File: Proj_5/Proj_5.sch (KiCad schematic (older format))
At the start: 1 part

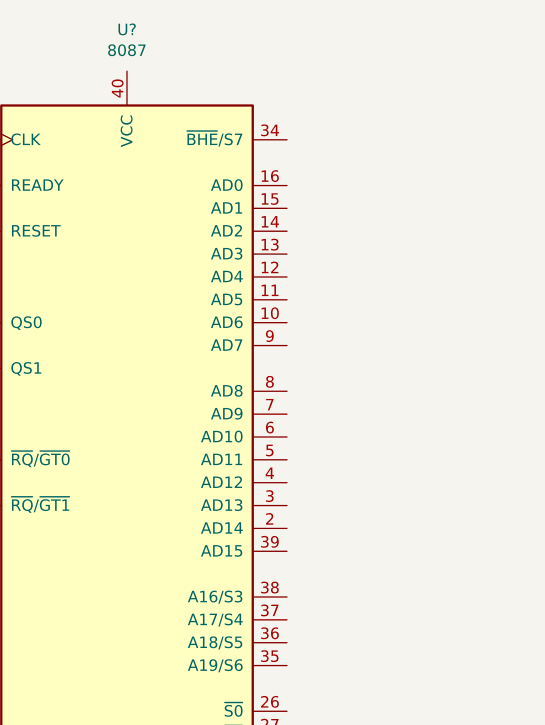
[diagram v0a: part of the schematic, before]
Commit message: Added Address Bus
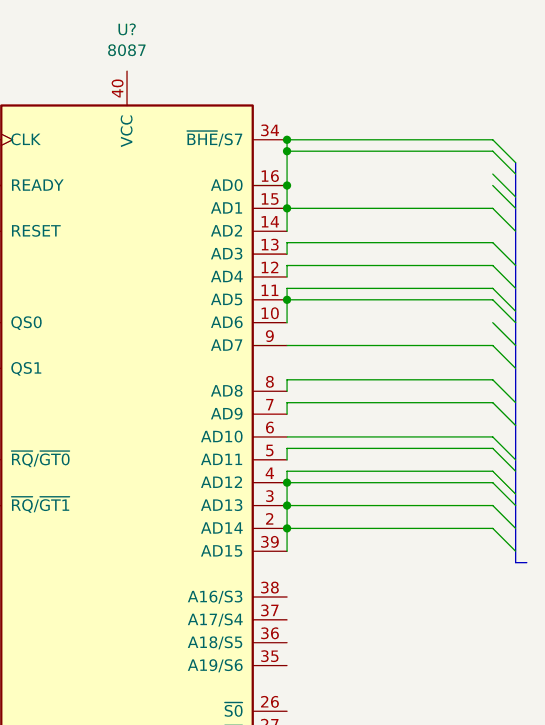
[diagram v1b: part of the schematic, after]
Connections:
- net at U?.10 (AD6): now also U?.11 (AD5)
- net at U?.14 (AD2): now also U?.15 (AD1), U?.16 (AD0), U?.34 (~BHE~/S7)
- net at U?.2 (AD14): now also U?.3 (AD13), U?.39 (AD15), U?.4 (AD12)
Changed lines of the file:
@@
 	1    0    0    -1
 $EndComp
+Wire Bus Line
+	3500 3250 3550 3250
+Entry Wire Line
+	3400 2300 3500 2400
+Entry Wire Line
+	3400 2450 3500 2550
+Entry Wire Line
+	3400 2550 3500 2650
+Entry Wire Line
+	3400 2700 3500 2800
+Entry Wire Line
+	3400 2750 3500 2850
+Entry Wire Line
+	3400 2850 3500 2950
+Entry Wire Line
+	3400 2900 3500 3000
+Entry Wire Line
+	3400 3000 3500 3100
+Entry Wire Line
+	3400 3100 3500 3200
+Entry Wire Line
+	3400 2200 3500 2300
+Entry Wire Line
+	3400 2100 3500 2200
+Entry Wire Line
+	3400 2050 3500 2150
+Entry Wire Line
+	3400 1950 3500 2050
+Entry Wire Line
+	3400 1850 3500 1950
+Entry Wire Line
+	3400 1700 3500 1800
+Entry Wire Line
+	3400 1600 3500 1700
+Entry Wire Line
+	3400 1450 3500 1550
+Entry Wire Line
+	3400 1400 3500 1500
+Entry Wire Line
+	3400 1550 3500 1650
+Wire Wire Line
+	3400 1400 2500 1400
+Connection ~ 2500 1400
+Wire Wire Line
+	3400 1450 2500 1450
+Wire Wire Line
+	2500 1400 2500 1450
+Connection ~ 2500 1450
+Wire Wire Line
+	2500 1450 2500 1600
+Connection ~ 2500 1600
+Wire Wire Line
+	2500 1600 2500 1700
+Wire Wire Line
+	3400 1850 2500 1850
+Wire Wire Line
+	2500 1850 2500 1900
+Wire Wire Line
+	3400 1700 2500 1700
+Wire Wire Line
+	2500 1700 2500 1800
+Connection ~ 2500 1700
+Wire Wire Line
+	3400 1950 2500 1950
+Wire Wire Line
+	2500 1950 2500 2000
+Wire Wire Line
+	3400 2050 2500 2050
+Wire Wire Line
+	2500 2050 2500 2100
+Wire Wire Line
+	3400 2100 2500 2100
+Wire Wire Line
+	2500 2100 2500 2200
+Connection ~ 2500 2100
+Wire Wire Line
+	3400 2300 2500 2300
+Wire Wire Line
+	3400 2450 2500 2450
+Wire Wire Line
+	2500 2450 2500 2500
+Wire Wire Line
+	3400 2550 2500 2550
+Wire Wire Line
+	2500 2550 2500 2600
+Wire Wire Line
+	3400 2700 2500 2700
+Wire Wire Line
+	3400 2750 2500 2750
+Wire Wire Line
+	2500 2750 2500 2800
+Wire Wire Line
+	3400 2850 2500 2850
+Wire Wire Line
+	2500 2850 2500 2900
+Wire Wire Line
+	3400 2900 2500 2900
+Wire Wire Line
+	2500 2900 2500 3000
+Connection ~ 2500 2900
+Wire Wire Line
+	3400 3000 2500 3000
+Wire Wire Line
+	2500 3000 2500 3100
+Connection ~ 2500 3000
+Wire Wire Line
+	3400 3100 2500 3100
+Wire Wire Line
+	2500 3100 2500 3200
+Wire Bus Line
+	3500 1500 3500 3250
+Connection ~ 2500 3100
 $EndSCHEMATC

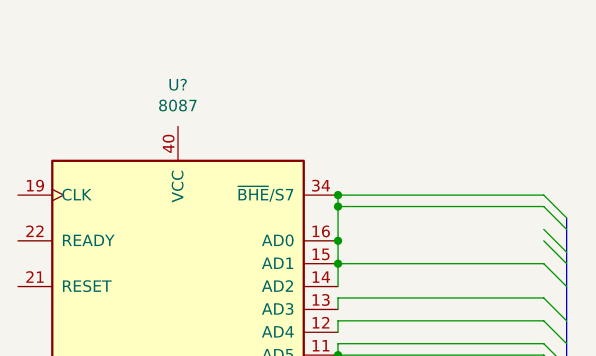
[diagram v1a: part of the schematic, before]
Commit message: Added Power to 8087
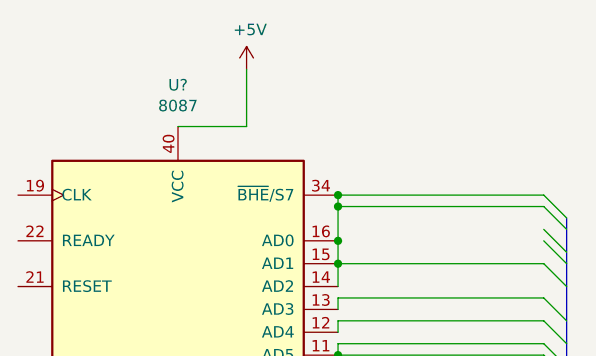
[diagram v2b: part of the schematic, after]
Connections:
- net +5V: now reaches U?.40 (VCC)
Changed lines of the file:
@@
 Wire Wire Line
 	2500 3100 2500 3200
+Connection ~ 2500 3100
+$Comp
+L power:+5V #PWR?
+U 1 1 5E90A12F
+P 2100 850
+F 0 "#PWR?" H 2100 700 50  0001 C CNN
+F 1 "+5V" H 2115 1023 50  0000 C CNN
+F 2 "" H 2100 850 50  0001 C CNN
+F 3 "" H 2100 850 50  0001 C CNN
+	1    2100 850
+	1    0    0    -1
+$EndComp
+Wire Wire Line
+	1800 1100 2100 1100
+Wire Wire Line
+	2100 1100 2100 850
 Wire Bus Line
 	3500 1500 3500 3250
-Connection ~ 2500 3100
 $EndSCHEMATC

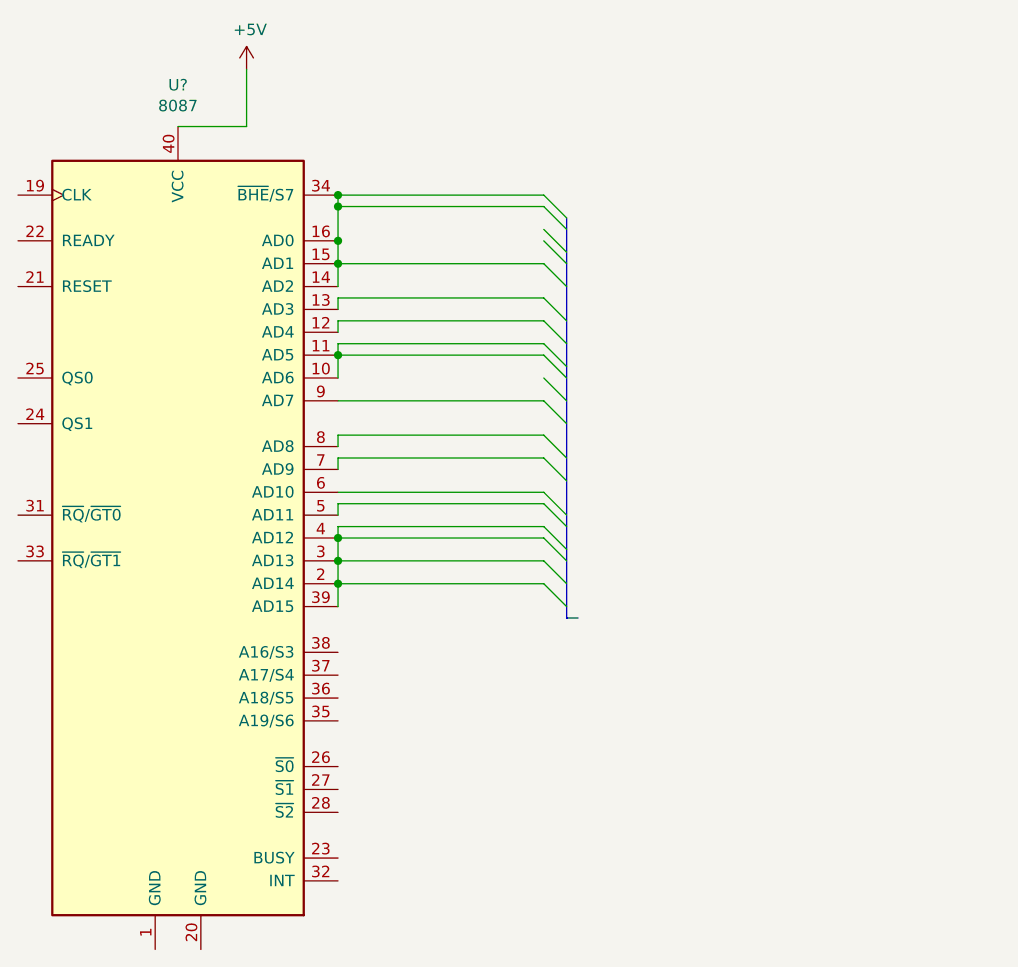
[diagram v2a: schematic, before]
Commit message: Added a clock circuit
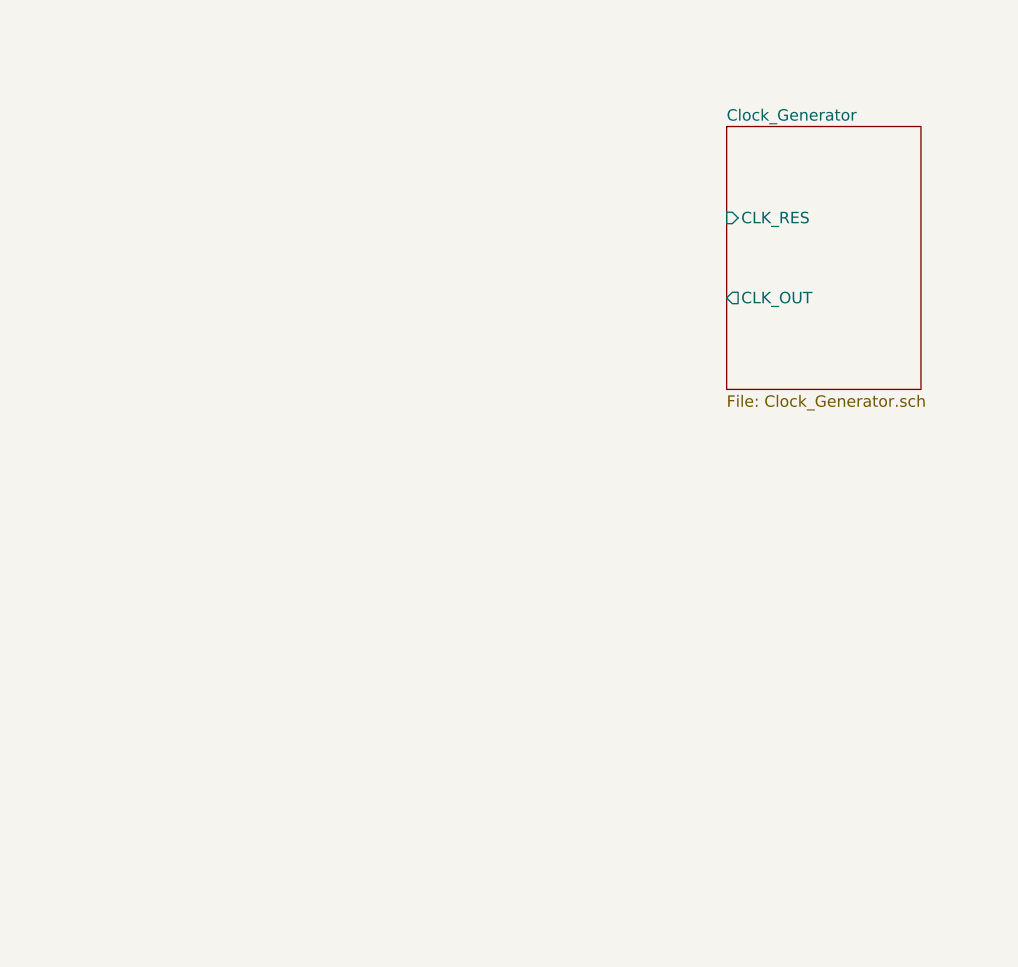
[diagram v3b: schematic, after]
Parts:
- removed U?: 8087, Package_DIP:DIP-40_W15.24mm, symbol MCU_Intel:8087
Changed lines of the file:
@@
 EELAYER 30 0
 EELAYER END
-$Descr A4 11693 8268
+$Descr User 19685 19685
 encoding utf-8
-Sheet 1 1
+Sheet 1 2
 Title ""
 Date ""
@@
 Comment4 ""
 $EndDescr
-$Comp
-L MCU_Intel:8087 U?
-U 1 1 5E90928D
-P 1800 2900
-F 0 "U?" H 1800 4881 50  0000 C CNN
-F 1 "8087" H 1800 4790 50  0000 C CNN
-F 2 "Package_DIP:DIP-40_W15.24mm" H 1850 3000 50  0001 C CIN
-F 3 "http://datasheets.chipdb.org/Intel/x86/808x/datashts/8087/205835-007.pdf" H 1800 2950 50  0001 C CNN
-	1    1800 2900
-	1    0    0    -1
-$EndComp
-Wire Bus Line
-	3500 3250 3550 3250
-Entry Wire Line
-	3400 2300 3500 2400
-Entry Wire Line
-	3400 2450 3500 2550
-Entry Wire Line
-	3400 2550 3500 2650
-Entry Wire Line
-	3400 2700 3500 2800
-Entry Wire Line
-	3400 2750 3500 2850
-Entry Wire Line
-	3400 2850 3500 2950
-Entry Wire Line
-	3400 2900 3500 3000
-Entry Wire Line
-	3400 3000 3500 3100
-Entry Wire Line
-	3400 3100 3500 3200
-Entry Wire Line
-	3400 2200 3500 2300
-Entry Wire Line
-	3400 2100 3500 2200
-Entry Wire Line
-	3400 2050 3500 2150
-Entry Wire Line
-	3400 1950 3500 2050
-Entry Wire Line
-	3400 1850 3500 1950
-Entry Wire Line
-	3400 1700 3500 1800
-Entry Wire Line
-	3400 1600 3500 1700
-Entry Wire Line
-	3400 1450 3500 1550
-Entry Wire Line
-	3400 1400 3500 1500
-Entry Wire Line
-	3400 1550 3500 1650
-Wire Wire Line
-	3400 1400 2500 1400
-Connection ~ 2500 1400
-Wire Wire Line
-	3400 1450 2500 1450
-Wire Wire Line
-	2500 1400 2500 1450
-Connection ~ 2500 1450
-Wire Wire Line
-	2500 1450 2500 1600
-Connection ~ 2500 1600
-Wire Wire Line
-	2500 1600 2500 1700
-Wire Wire Line
-	3400 1850 2500 1850
-Wire Wire Line
-	2500 1850 2500 1900
-Wire Wire Line
-	3400 1700 2500 1700
-Wire Wire Line
-	2500 1700 2500 1800
-Connection ~ 2500 1700
-Wire Wire Line
-	3400 1950 2500 1950
-Wire Wire Line
-	2500 1950 2500 2000
-Wire Wire Line
-	3400 2050 2500 2050
-Wire Wire Line
-	2500 2050 2500 2100
-Wire Wire Line
-	3400 2100 2500 2100
-Wire Wire Line
-	2500 2100 2500 2200
-Connection ~ 2500 2100
-Wire Wire Line
-	3400 2300 2500 2300
-Wire Wire Line
-	3400 2450 2500 2450
-Wire Wire Line
-	2500 2450 2500 2500
-Wire Wire Line
-	3400 2550 2500 2550
-Wire Wire Line
-	2500 2550 2500 2600
-Wire Wire Line
-	3400 2700 2500 2700
-Wire Wire Line
-	3400 2750 2500 2750
-Wire Wire Line
-	2500 2750 2500 2800
-Wire Wire Line
-	3400 2850 2500 2850
-Wire Wire Line
-	2500 2850 2500 2900
-Wire Wire Line
-	3400 2900 2500 2900
-Wire Wire Line
-	2500 2900 2500 3000
-Connection ~ 2500 2900
-Wire Wire Line
-	3400 3000 2500 3000
-Wire Wire Line
-	2500 3000 2500 3100
-Connection ~ 2500 3000
-Wire Wire Line
-	3400 3100 2500 3100
-Wire Wire Line
-	2500 3100 2500 3200
-Connection ~ 2500 3100
-$Comp
-L power:+5V #PWR?
-U 1 1 5E90A12F
-P 2100 850
-F 0 "#PWR?" H 2100 700 50  0001 C CNN
-F 1 "+5V" H 2115 1023 50  0000 C CNN
-F 2 "" H 2100 850 50  0001 C CNN
-F 3 "" H 2100 850 50  0001 C CNN
-	1    2100 850
-	1    0    0    -1
-$EndComp
-Wire Wire Line
-	1800 1100 2100 1100
-Wire Wire Line
-	2100 1100 2100 850
-Wire Bus Line
-	3500 1500 3500 3250
+$Sheet
+S 4200 1100 850  1150
+U 5E9E2E0E
+F0 "Clock_Generator" 50
+F1 "Clock_Generator.sch" 50
+F2 "CLK_RES" I L 4200 1500 50
+F3 "CLK_OUT" O L 4200 1850 50
+$EndSheet
 $EndSCHEMATC

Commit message: Added Schematics, finish SRAM and 8279
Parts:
- added U?: 8086_Min_Mode, Package_DIP:DIP-40_W15.24mm, symbol MCU_Intel:8086_Min_Mode
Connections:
- net Clock_Generator/CLK_OUT: now also U?.19 (CLK)
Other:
- note added: "Ryan Bugianesi and Collin Mood\n"
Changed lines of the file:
@@
 $Descr User 19685 19685
 encoding utf-8
-Sheet 1 2
+Sheet 1 9
 Title ""
 Date ""
@@
 $EndDescr
 $Sheet
-S 4200 1100 850  1150
+S 1150 800  850  1150
 U 5E9E2E0E
 F0 "Clock_Generator" 50
 F1 "Clock_Generator.sch" 50
-F2 "CLK_RES" I L 4200 1500 50
-F3 "CLK_OUT" O L 4200 1850 50
+F2 "CLK_RES" I L 1150 1200 50
+F3 "CLK_OUT" O L 1150 1550 50
 $EndSheet
+$Comp
+L MCU_Intel:8086_Min_Mode U?
+U 1 1 5E99BD91
+P 3200 4050
+F 0 "U?" H 3200 6031 50  0000 C CNN
+F 1 "8086_Min_Mode" H 3200 5940 50  0000 C CNN
+F 2 "Package_DIP:DIP-40_W15.24mm" H 3250 4150 50  0001 C CIN
+F 3 "http://datasheets.chipdb.org/Intel/x86/808x/datashts/8086/231455-006.pdf" H 3200 4100 50  0001 C CNN
+	1    3200 4050
+	1    0    0    -1
+$EndComp
+Wire Wire Line
+	1150 1550 750  1550
+Wire Wire Line
+	750  1550 750  2550
+Wire Wire Line
+	750  2550 2500 2550
+$Sheet
+S 13550 4000 2500 1950
+U 5EA0416B
+F0 "8255s" 157
+F1 "8255s.sch" 157
+$EndSheet
+$Sheet
+S 13500 1000 2500 2250
+U 5EA045EA
+F0 "CMOS Flash" 157
+F1 "CMOS-28F010s.sch" 157
+$EndSheet
+$Sheet
+S 13550 6850 2600 2600
+U 5EA98353
+F0 "SRAM Memory" 256
+F1 "CY7C199.sch" 256
+$EndSheet
+$Sheet
+S 13750 11050 2450 2500
+U 5EA98A67
+F0 "16550 UART" 256
+F1 "16550UART.sch" 256
+$EndSheet
+$Sheet
+S 8200 14600 3250 2700
+U 5EA99014
+F0 "8259" 256
+F1 "8259.sch" 256
+$EndSheet
+$Sheet
+S 13850 14800 3400 2350
+U 5EA99146
+F0 "8254" 256
+F1 "8254.sch" 256
+$EndSheet
+$Sheet
+S 3900 14900 3050 2250
+U 5EA993EC
+F0 "8279" 256
+F1 "8279.sch" 256
+$EndSheet
+Text Notes 14950 18250 0    169  ~ 0
+Ryan Bugianesi and Collin Mood\n
 $EndSCHEMATC

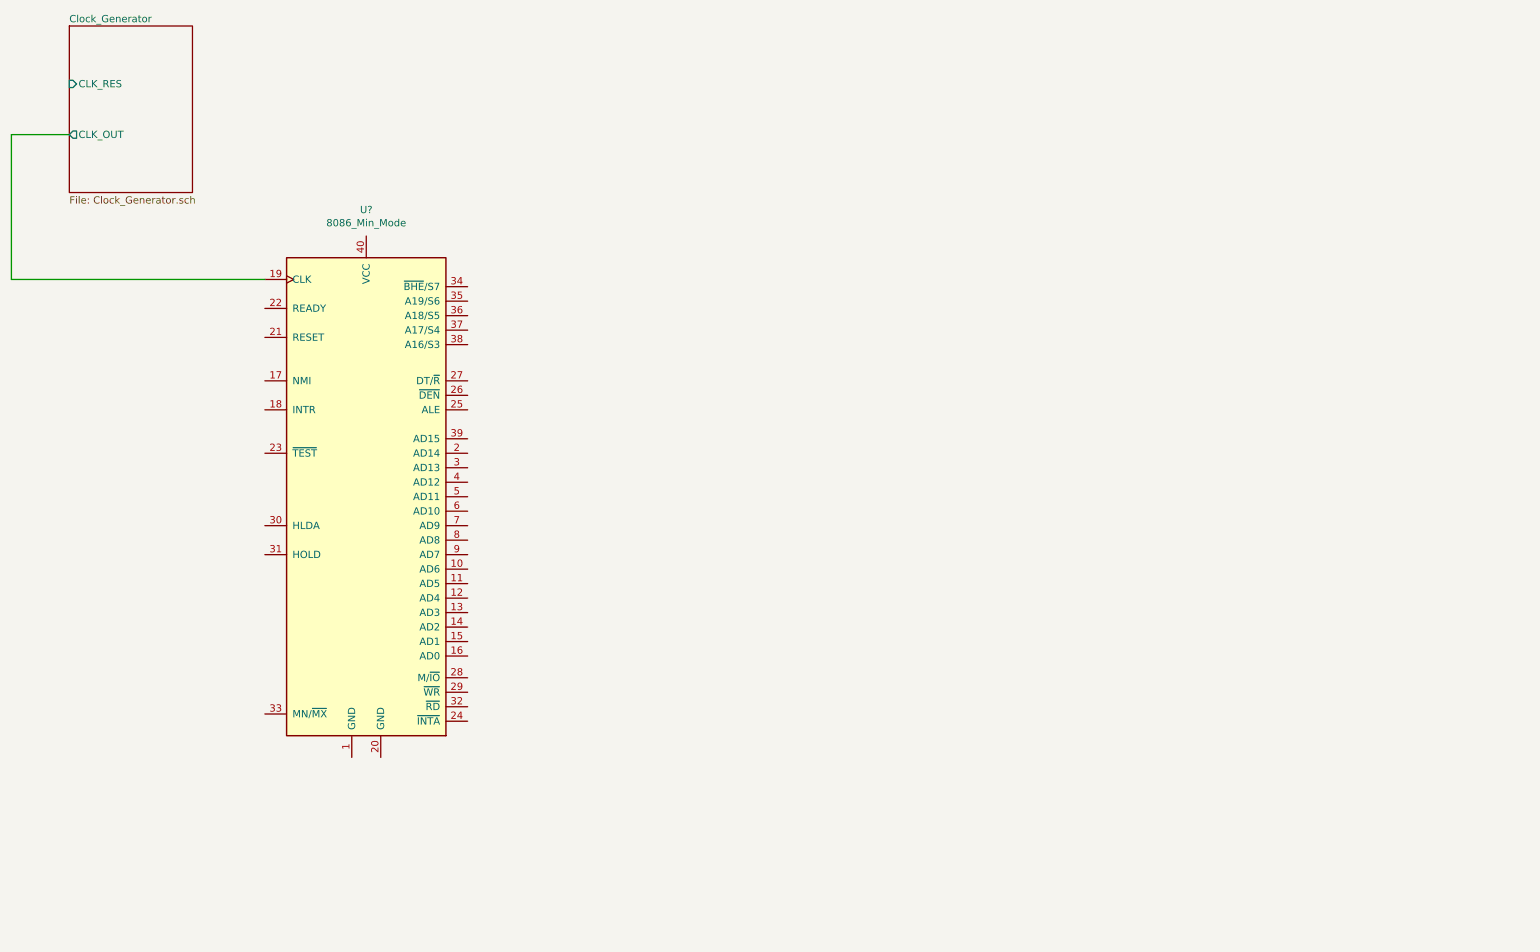
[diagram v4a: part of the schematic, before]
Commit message: Placed 8086 in own Sheet
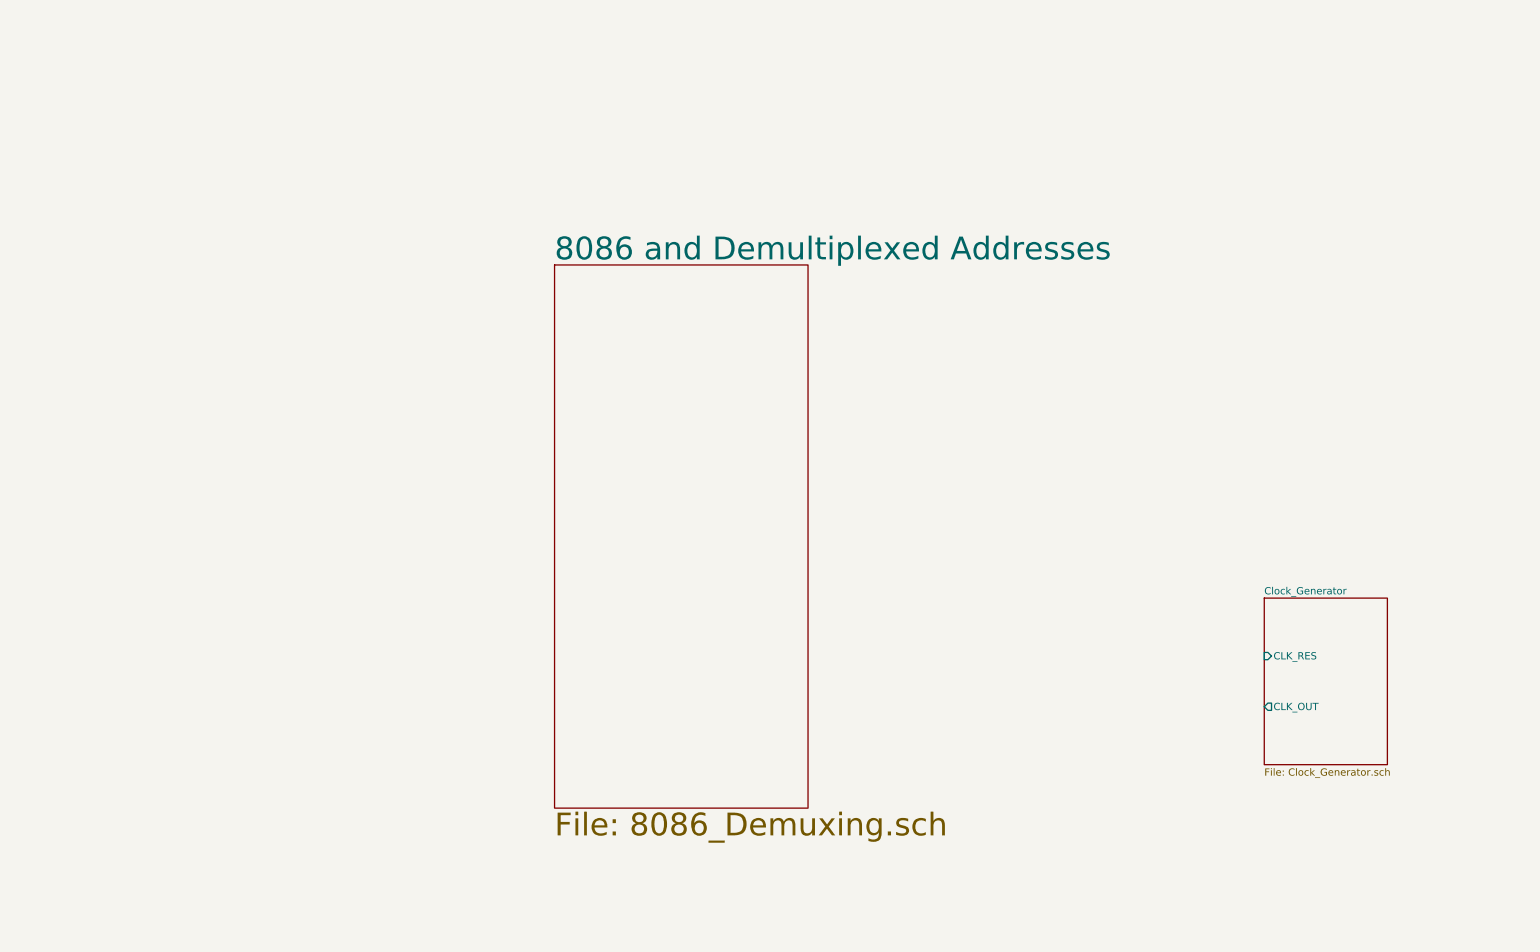
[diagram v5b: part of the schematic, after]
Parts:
- removed U?: 8086_Min_Mode, Package_DIP:DIP-40_W15.24mm, symbol MCU_Intel:8086_Min_Mode
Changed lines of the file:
@@
 $Descr User 19685 19685
 encoding utf-8
-Sheet 1 9
+Sheet 1 10
 Title ""
 Date ""
@@
 $EndDescr
 $Sheet
-S 1150 800  850  1150
+S 9400 4750 850  1150
 U 5E9E2E0E
 F0 "Clock_Generator" 50
 F1 "Clock_Generator.sch" 50
-F2 "CLK_RES" I L 1150 1200 50
-F3 "CLK_OUT" O L 1150 1550 50
+F2 "CLK_RES" I L 9400 5150 50
+F3 "CLK_OUT" O L 9400 5500 50
 $EndSheet
-$Comp
-L MCU_Intel:8086_Min_Mode U?
-U 1 1 5E99BD91
-P 3200 4050
-F 0 "U?" H 3200 6031 50  0000 C CNN
-F 1 "8086_Min_Mode" H 3200 5940 50  0000 C CNN
-F 2 "Package_DIP:DIP-40_W15.24mm" H 3250 4150 50  0001 C CIN
-F 3 "http://datasheets.chipdb.org/Intel/x86/808x/datashts/8086/231455-006.pdf" H 3200 4100 50  0001 C CNN
-	1    3200 4050
-	1    0    0    -1
-$EndComp
-Wire Wire Line
-	1150 1550 750  1550
-Wire Wire Line
-	750  1550 750  2550
-Wire Wire Line
-	750  2550 2500 2550
 $Sheet
 S 13550 4000 2500 1950
@@
 Text Notes 14950 18250 0    169  ~ 0
 Ryan Bugianesi and Collin Mood\n
+$Sheet
+S 4500 2450 1750 3750
+U 5E9F3A3D
+F0 "8086 and Demultiplexed Addresses" 157
+F1 "8086_Demuxing.sch" 157
+$EndSheet
 $EndSCHEMATC
